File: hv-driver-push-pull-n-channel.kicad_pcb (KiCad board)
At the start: 2 copper layers, 25.7 x 18.5 mm, 10 parts, among them P1 CONN_01X04, P2 CONN_01X03, Q1 BSS127S-7, Q2 BSS127S-7, U1 NCP5304

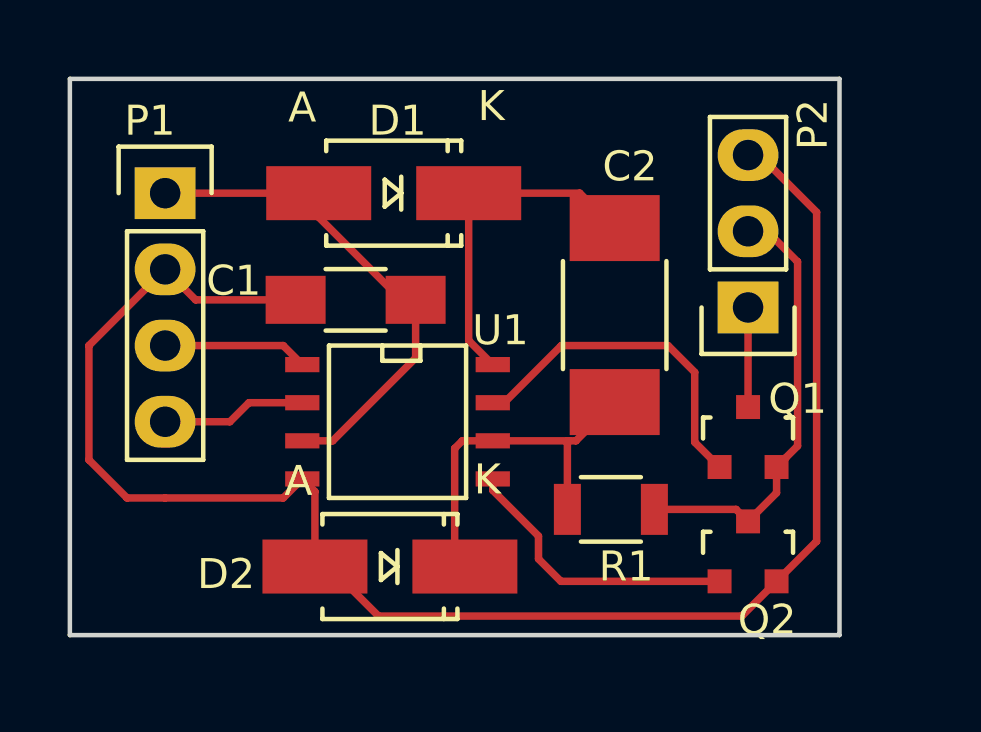
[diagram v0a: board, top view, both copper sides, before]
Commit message: Put header pins on 0.1in grid
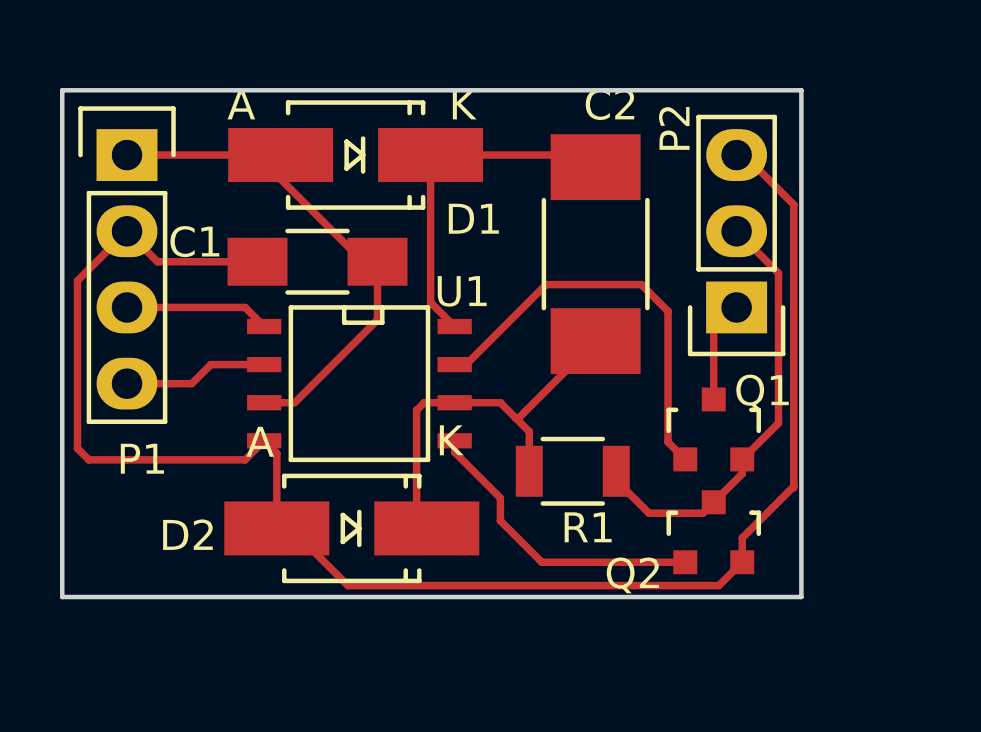
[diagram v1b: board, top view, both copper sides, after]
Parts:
- moved C2 2.13 mm to (142.6, 104.9)
- moved P1 1.80 mm to (127.0, 101.6)
- moved C1 1.80 mm to (133.3, 105.2)
- moved D2 1.80 mm to (134.5, 114.0)
- moved D1 1.80 mm to (134.6, 101.6)
- moved R1 1.80 mm to (141.9, 112.1)
- moved U1 1.80 mm to (134.7, 109.2)
- moved Q2 1.31 mm to (146.6, 114.2)
- moved Q1 1.17 mm to (146.6, 110.7)
- moved P2 0.38 mm to (147.3, 106.7)
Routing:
- net Net-(Q1-Pad1): track 11.4 -> 13.8 mm
- net GND: track 55.7 -> 54.3 mm
- net Net-(C2-Pad1): track 12.4 -> 13.4 mm
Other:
- board size 25.7 x 18.5 mm -> 24.6 x 16.9 mm

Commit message: Make compatible with CNC milling
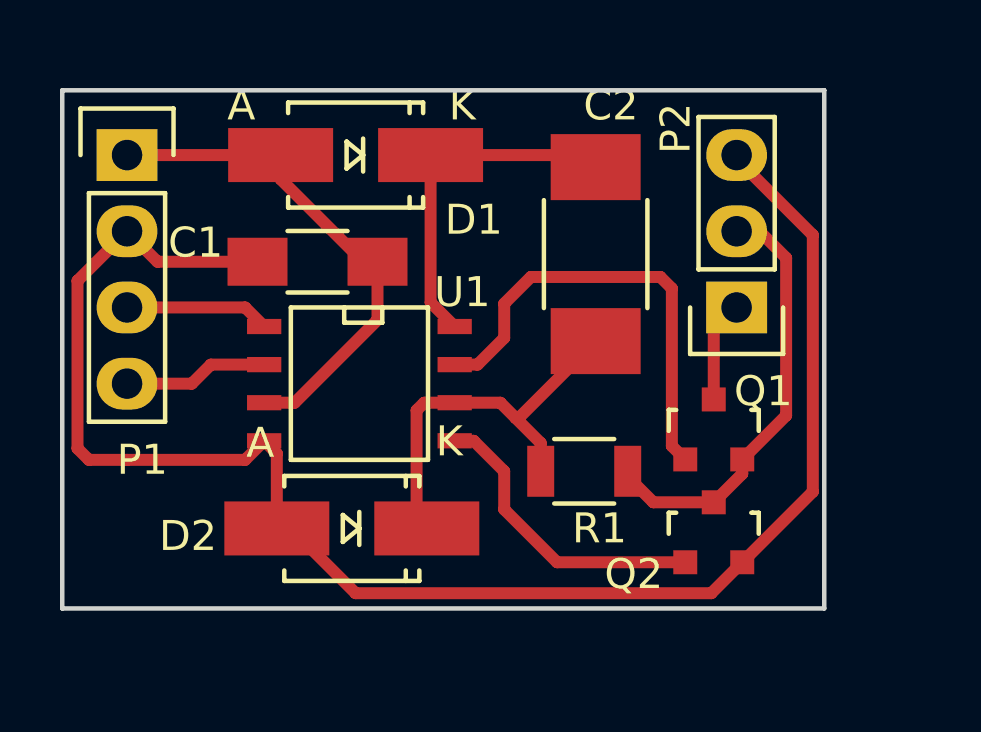
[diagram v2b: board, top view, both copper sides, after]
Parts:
- moved R1 0.38 mm to (142.2, 112.1)
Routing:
- net Net-(Q1-Pad1): track 13.8 -> 15.5 mm
- net GND: track 54.3 -> 55.5 mm
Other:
- board size 24.6 x 16.9 mm -> 25.4 x 17.3 mm
- net class Default: clearance 0.2 -> 0.4; trace_width 0.25 -> 0.4
- rule trace_clearance: 0.2 -> 0.4

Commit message: Change length to match main board and add fuse
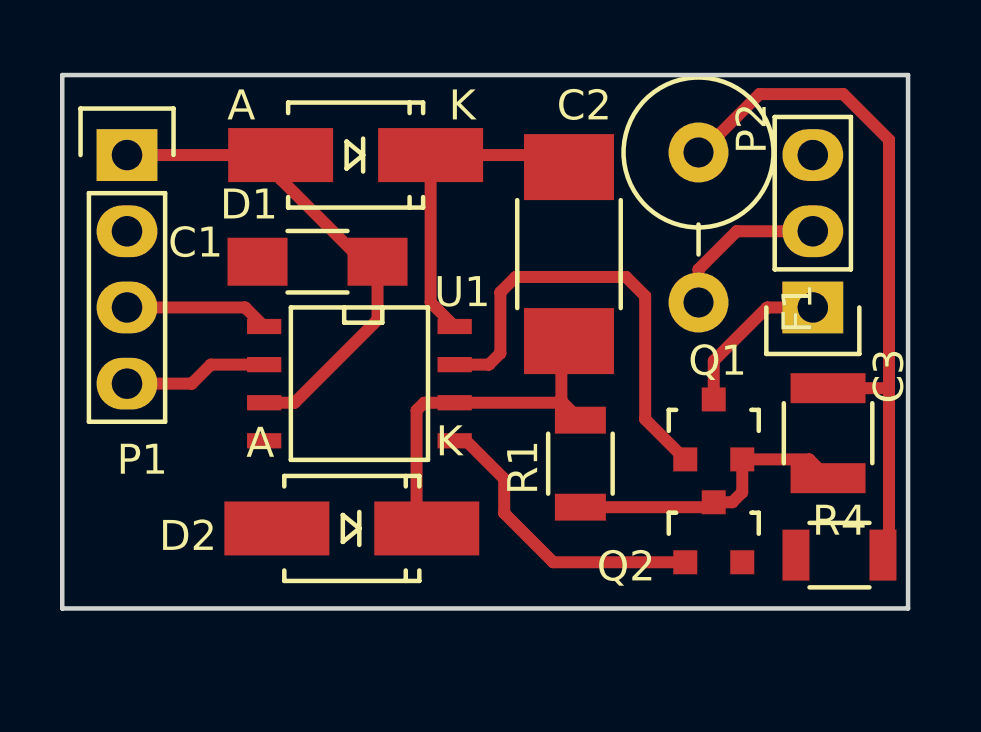
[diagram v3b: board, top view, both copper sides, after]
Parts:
- added C3: C, Capacitors_SMD:C_1210, F.Cu at (150.4, 110.9)
- added F1: FUSE, Resistors_ThroughHole:Resistor_Vertical_RM5mm, F.Cu at (146.1, 104.0)
- added R4: R, Resistors_SMD:R_1206, F.Cu at (150.7, 114.9)
- moved P2 2.54 mm to (149.9, 106.7)
- moved C2 0.89 mm to (141.7, 104.9)
- moved R1 0.28 mm to (142.1, 111.9), turned to 90 degrees
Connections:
- P2 pad 2: OUT -> Net-(F1-Pad2)
- Q1 pad 2: OUT -> Net-(C3-Pad1)
- Q2 pad 3: OUT -> Net-(C3-Pad1)
- R1 pad 1: OUT -> Net-(C3-Pad1)
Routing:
- net GND: track 55.5 -> 0.47 mm
- net Net-(C3-Pad1): track 0.00 -> 9.82 mm
- net OUT: track 14.6 -> 23.8 mm
- net Net-(F1-Pad2): track 0.00 -> 5.44 mm
- net HV: track 3.38 -> 5.33 mm
- net Net-(C2-Pad1): track 13.5 -> 12.0 mm
- net Net-(C2-Pad2): track 11.7 -> 10.8 mm
- added copper zone on F.Cu, net GND
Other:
- board size 25.4 x 17.3 mm -> 28.2 x 17.8 mm

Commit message: Use T220 transistors and add gate resistors
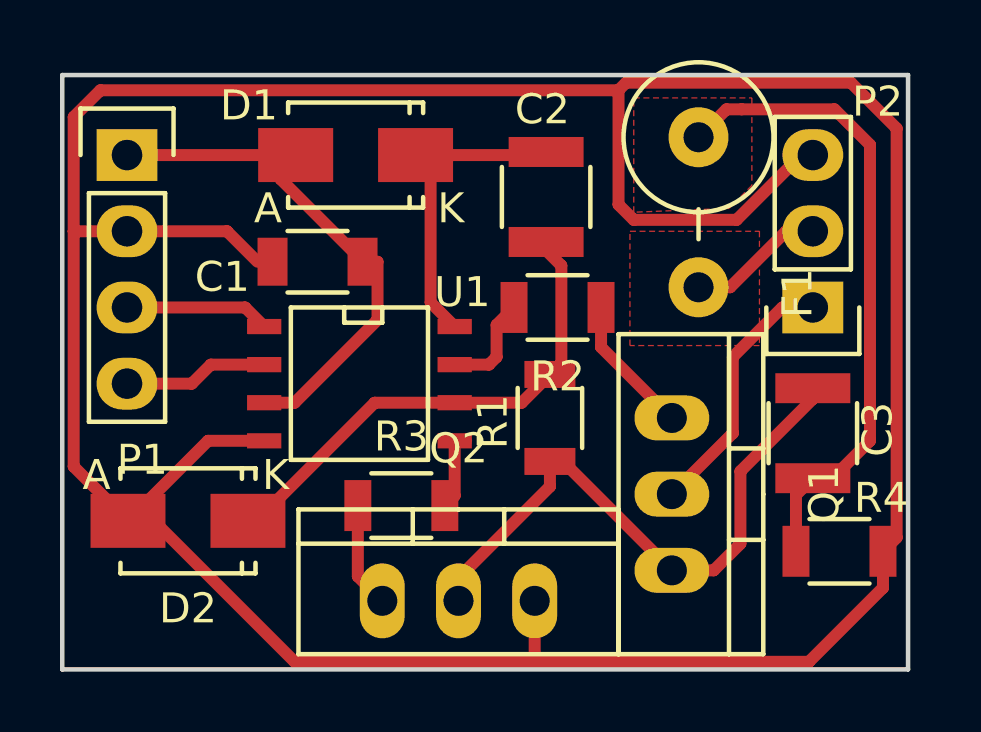
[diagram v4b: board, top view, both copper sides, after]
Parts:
- added R2: 10, Resistors_SMD:R_1206, F.Cu at (141.4, 106.7)
- added R3: 10, Resistors_SMD:R_1206, F.Cu at (136.1, 113.3)
- C1: footprint Capacitors_SMD:C_1206_HandSoldering -> Capacitors_SMD:C_1206
- C2: footprint Capacitors_SMD:C_1812_HandSoldering -> Capacitors_SMD:C_1210
- D1, D2: footprint Diodes_SMD:SMA_Handsoldering -> Diodes_SMD:SMA_Standard
- Q1, Q2: value BSS127S-7 -> Q_NMOS_GDS; footprint TO_SOT_Packages_SMD:SOT-23 -> TO_SOT_Packages_THT:TO-220_Neutral123_Vertical
- moved Q2 8.81 mm to (138.0, 116.5)
- moved D2 5.47 mm to (129.0, 113.8)
- moved Q1 2.57 mm to (145.2, 112.9), turned to 270 degrees
- moved C2 2.05 mm to (141.0, 103.0)
- moved R1 1.83 mm to (141.1, 110.4)
- moved F1 0.51 mm to (146.1, 103.5)
- moved C3 0.51 mm to (149.9, 110.9), turned to 270 degrees
- moved R4 0.13 mm to (150.7, 114.8), turned to 0 degrees
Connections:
- Q1 pad 2: Net-(C3-Pad1) -> HV
- Q1 pad 3: HV -> Net-(C3-Pad1)
- Q2 pad 2: GND -> Net-(C3-Pad1)
- Q2 pad 3: Net-(C3-Pad1) -> GND
- U1 pad 5: Net-(Q2-Pad1) -> Net-(R3-Pad2)
- U1 pad 7: Net-(Q1-Pad1) -> Net-(R2-Pad2)
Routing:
- net GND: track 0.47 -> 112.8 mm
- net Net-(C3-Pad1): track 9.82 -> 22.3 mm
- net Net-(Q1-Pad1): track 15.7 -> 4.66 mm
- net Net-(Q2-Pad1): track 10.0 -> 3.51 mm
- net Net-(C2-Pad1): track 12.0 -> 17.5 mm
- net HV: track 5.33 -> 9.40 mm
- net Net-(R2-Pad2): track 0.00 -> 3.78 mm
- net Net-(R3-Pad2): track 0.00 -> 2.68 mm
- net OUT: track 23.8 -> 21.6 mm
- net Net-(F1-Pad2): track 5.44 -> 4.58 mm
- added copper zone on F.Cu, net Net-(F1-Pad2)
- added copper zone on F.Cu, net OUT
- removed copper zone on F.Cu, net GND
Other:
- board size 28.2 x 17.8 mm -> 28.2 x 19.8 mm

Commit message: Remove gate resistors
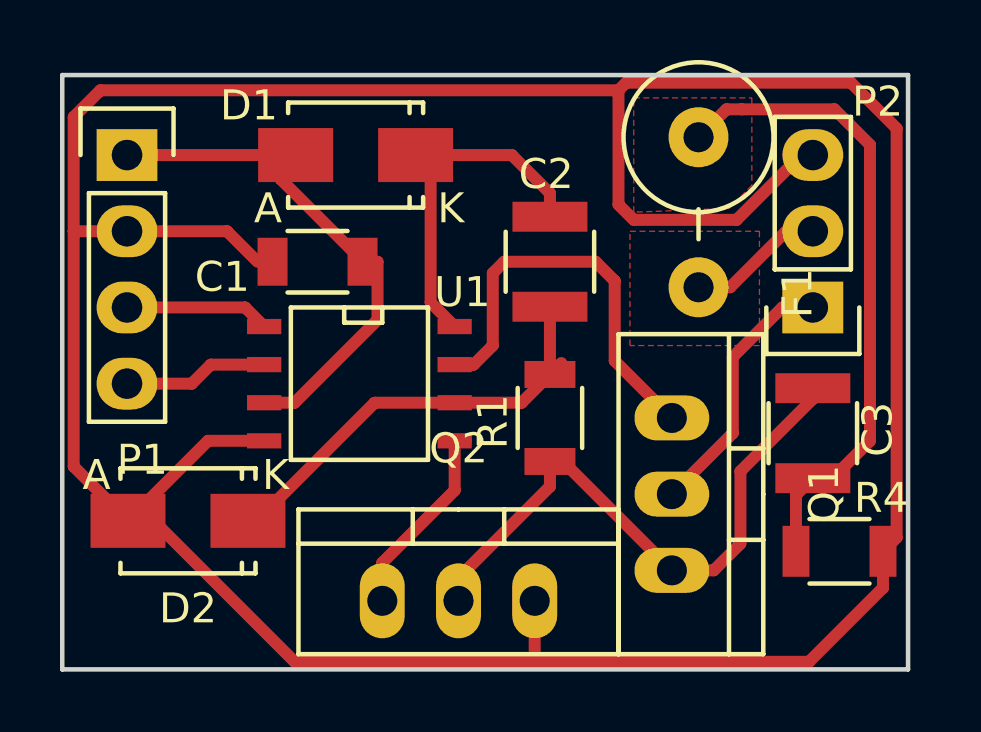
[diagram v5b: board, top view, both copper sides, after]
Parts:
- removed R2, R3: 10, Resistors_SMD:R_1206
- moved C2 2.16 mm to (141.1, 105.2)
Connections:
- U1 pad 5: Net-(R3-Pad2) -> Net-(Q2-Pad1)
- U1 pad 7: Net-(R2-Pad2) -> Net-(Q1-Pad1)
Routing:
- net Net-(Q1-Pad1): track 4.66 -> 14.2 mm
- net Net-(R2-Pad2): track 3.78 -> 0.00 mm
- net Net-(Q2-Pad1): track 3.51 -> 6.71 mm
- net Net-(R3-Pad2): track 2.68 -> 0.00 mm
- net Net-(C2-Pad1): track 17.5 -> 15.5 mm
- net Net-(C2-Pad2): track 10.4 -> 11.8 mm
